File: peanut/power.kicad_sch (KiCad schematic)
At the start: 17 parts, among them J3 Battery JST, J4 Arming, Q5 PMOS, U4 MCP1826S, U5 TPS2116DRL

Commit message: feat: changed pressure sensor to BMP581
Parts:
- renumbered C15 to C16, C16 to C17, C17 to C18, C18 to C19, C19 to C20
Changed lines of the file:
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@@
 		(dnp no)
 		(fields_autoplaced yes)
-		(property "Reference" "C17"
+		(property "Reference" "C18"
 			(at 114.3 83.8199 0)
 			(show_name no)
@@
 			(project "peanut"
 				(path "/5c6b6cfc-6c84-425a-9b66-e6111713aae8/f944ce75-1da7-4030-9ed2-502ac98b17ed"
-					(reference "C17")
+					(reference "C18")
 					(unit 1)
 				)
@@
 		(dnp no)
 		(fields_autoplaced yes)
-		(property "Reference" "#PWR058"
+		(property "Reference" "#PWR061"
 			(at 232.41 80.01 0)
 			(hide yes)
@@
 			(project "peanut"
 				(path "/5c6b6cfc-6c84-425a-9b66-e6111713aae8/f944ce75-1da7-4030-9ed2-502ac98b17ed"
-					(reference "#PWR058")
+					(reference "#PWR061")
 					(unit 1)
 				)
@@
 		(dnp no)
 		(fields_autoplaced yes)
-		(property "Reference" "#PWR054"
+		(property "Reference" "#PWR057"
 			(at 163.83 77.47 0)
 			(hide yes)
@@
 			(project "peanut"
 				(path "/5c6b6cfc-6c84-425a-9b66-e6111713aae8/f944ce75-1da7-4030-9ed2-502ac98b17ed"
-					(reference "#PWR054")
+					(reference "#PWR057")
 					(unit 1)
 				)
@@
 		(dnp no)
 		(fields_autoplaced yes)
-		(property "Reference" "#PWR047"
+		(property "Reference" "#PWR050"
 			(at 105.41 72.39 0)
 			(hide yes)
@@
 			(project "peanut"
 				(path "/5c6b6cfc-6c84-425a-9b66-e6111713aae8/f944ce75-1da7-4030-9ed2-502ac98b17ed"
-					(reference "#PWR047")
+					(reference "#PWR050")
 					(unit 1)
 				)
@@
 		(dnp no)
 		(fields_autoplaced yes)
-		(property "Reference" "#PWR053"
+		(property "Reference" "#PWR056"
 			(at 139.7 92.71 0)
 			(hide yes)
@@
 			(project "peanut"
 				(path "/5c6b6cfc-6c84-425a-9b66-e6111713aae8/f944ce75-1da7-4030-9ed2-502ac98b17ed"
-					(reference "#PWR053")
+					(reference "#PWR056")
 					(unit 1)
 				)
@@
 		(in_pos_files yes)
 		(dnp no)
-		(property "Reference" "#PWR057"
+		(property "Reference" "#PWR060"
 			(at 231.14 71.12 0)
 			(hide yes)
@@
 			(project "peanut"
 				(path "/5c6b6cfc-6c84-425a-9b66-e6111713aae8/f944ce75-1da7-4030-9ed2-502ac98b17ed"
-					(reference "#PWR057")
+					(reference "#PWR060")
 					(unit 1)
 				)
@@
 		(dnp no)
 		(fields_autoplaced yes)
-		(property "Reference" "#PWR051"
+		(property "Reference" "#PWR054"
 			(at 116.84 140.97 0)
 			(hide yes)
@@
 			(project "peanut"
 				(path "/5c6b6cfc-6c84-425a-9b66-e6111713aae8/f944ce75-1da7-4030-9ed2-502ac98b17ed"
-					(reference "#PWR051")
+					(reference "#PWR054")
 					(unit 1)
 				)
@@
 		(in_pos_files yes)
 		(dnp no)
-		(property "Reference" "#PWR048"
+		(property "Reference" "#PWR051"
 			(at 105.41 83.82 0)
 			(hide yes)
@@
 			(project "peanut"
 				(path "/5c6b6cfc-6c84-425a-9b66-e6111713aae8/f944ce75-1da7-4030-9ed2-502ac98b17ed"
-					(reference "#PWR048")
+					(reference "#PWR051")
 					(unit 1)
 				)
@@
 		(dnp no)
 		(fields_autoplaced yes)
-		(property "Reference" "#PWR056"
+		(property "Reference" "#PWR059"
 			(at 199.39 71.12 0)
 			(hide yes)
@@
 			(project "peanut"
 				(path "/5c6b6cfc-6c84-425a-9b66-e6111713aae8/f944ce75-1da7-4030-9ed2-502ac98b17ed"
-					(reference "#PWR056")
+					(reference "#PWR059")
 					(unit 1)
 				)
@@
 		(in_pos_files yes)
 		(dnp no)
-		(property "Reference" "C15"
+		(property "Reference" "C16"
 			(at 45.212 71.12 0)
 			(show_name no)
@@
 			(project "peanut"
 				(path "/5c6b6cfc-6c84-425a-9b66-e6111713aae8/f944ce75-1da7-4030-9ed2-502ac98b17ed"
-					(reference "C15")
+					(reference "C16")
 					(unit 1)
 				)
@@
 		(in_pos_files yes)
 		(dnp no)
-		(property "Reference" "#PWR041"
+		(property "Reference" "#PWR044"
 			(at 43.18 102.87 0)
 			(hide yes)
@@
 			(project "peanut"
 				(path "/5c6b6cfc-6c84-425a-9b66-e6111713aae8/f944ce75-1da7-4030-9ed2-502ac98b17ed"
-					(reference "#PWR041")
+					(reference "#PWR044")
 					(unit 1)
 				)
@@
 		(dnp no)
 		(fields_autoplaced yes)
-		(property "Reference" "C18"
+		(property "Reference" "C19"
 			(at 121.92 73.6599 0)
 			(show_name no)
@@
 			(project "peanut"
 				(path "/5c6b6cfc-6c84-425a-9b66-e6111713aae8/f944ce75-1da7-4030-9ed2-502ac98b17ed"
-					(reference "C18")
+					(reference "C19")
 					(unit 1)
 				)
@@
 		(dnp no)
 		(fields_autoplaced yes)
-		(property "Reference" "#PWR055"
+		(property "Reference" "#PWR058"
 			(at 198.12 76.2 0)
 			(hide yes)
@@
 			(project "peanut"
 				(path "/5c6b6cfc-6c84-425a-9b66-e6111713aae8/f944ce75-1da7-4030-9ed2-502ac98b17ed"
-					(reference "#PWR055")
+					(reference "#PWR058")
 					(unit 1)
 				)
@@
 		(dnp no)
 		(fields_autoplaced yes)
-		(property "Reference" "#PWR052"
+		(property "Reference" "#PWR055"
 			(at 127 119.38 0)
 			(hide yes)
@@
 			(project "peanut"
 				(path "/5c6b6cfc-6c84-425a-9b66-e6111713aae8/f944ce75-1da7-4030-9ed2-502ac98b17ed"
-					(reference "#PWR052")
+					(reference "#PWR055")
 					(unit 1)
 				)
@@
 		(dnp no)
 		(fields_autoplaced yes)
-		(property "Reference" "#PWR046"
+		(property "Reference" "#PWR049"
 			(at 86.36 72.39 0)
 			(hide yes)
@@
 			(project "peanut"
 				(path "/5c6b6cfc-6c84-425a-9b66-e6111713aae8/f944ce75-1da7-4030-9ed2-502ac98b17ed"
-					(reference "#PWR046")
+					(reference "#PWR049")
 					(unit 1)
 				)
@@
 		(in_pos_files yes)
 		(dnp no)
-		(property "Reference" "#PWR049"
+		(property "Reference" "#PWR052"
 			(at 109.22 119.38 0)
 			(hide yes)
@@
 			(project "peanut"
 				(path "/5c6b6cfc-6c84-425a-9b66-e6111713aae8/f944ce75-1da7-4030-9ed2-502ac98b17ed"
-					(reference "#PWR049")
+					(reference "#PWR052")
 					(unit 1)
 				)
@@
 		(dnp no)
 		(fields_autoplaced yes)
-		(property "Reference" "#PWR045"
+		(property "Reference" "#PWR048"
 			(at 82.55 119.38 0)
 			(hide yes)
@@
 			(project "peanut"
 				(path "/5c6b6cfc-6c84-425a-9b66-e6111713aae8/f944ce75-1da7-4030-9ed2-502ac98b17ed"
-					(reference "#PWR045")
+					(reference "#PWR048")
 					(unit 1)
 				)
@@
 		(dnp no)
 		(fields_autoplaced yes)
-		(property "Reference" "C16"
+		(property "Reference" "C17"
 			(at 90.17 71.1199 0)
 			(show_name no)
@@
 			(project "peanut"
 				(path "/5c6b6cfc-6c84-425a-9b66-e6111713aae8/f944ce75-1da7-4030-9ed2-502ac98b17ed"
-					(reference "C16")
+					(reference "C17")
 					(unit 1)
 				)
@@
 		(dnp no)
 		(fields_autoplaced yes)
-		(property "Reference" "#PWR042"
+		(property "Reference" "#PWR045"
 			(at 53.34 114.3 0)
 			(hide yes)
@@
 			(project "peanut"
 				(path "/5c6b6cfc-6c84-425a-9b66-e6111713aae8/f944ce75-1da7-4030-9ed2-502ac98b17ed"
-					(reference "#PWR042")
+					(reference "#PWR045")
 					(unit 1)
 				)
@@
 		(dnp no)
 		(fields_autoplaced yes)
-		(property "Reference" "#PWR044"
+		(property "Reference" "#PWR047"
 			(at 82.55 101.6 0)
 			(hide yes)
@@
 			(project "peanut"
 				(path "/5c6b6cfc-6c84-425a-9b66-e6111713aae8/f944ce75-1da7-4030-9ed2-502ac98b17ed"
-					(reference "#PWR044")
+					(reference "#PWR047")
 					(unit 1)
 				)
@@
 		(dnp no)
 		(fields_autoplaced yes)
-		(property "Reference" "#PWR043"
+		(property "Reference" "#PWR046"
 			(at 67.31 83.82 0)
 			(hide yes)
@@
 			(project "peanut"
 				(path "/5c6b6cfc-6c84-425a-9b66-e6111713aae8/f944ce75-1da7-4030-9ed2-502ac98b17ed"
-					(reference "#PWR043")
+					(reference "#PWR046")
 					(unit 1)
 				)
@@
 		(dnp no)
 		(fields_autoplaced yes)
-		(property "Reference" "#PWR050"
+		(property "Reference" "#PWR053"
 			(at 114.3 95.25 0)
 			(hide yes)
@@
 			(project "peanut"
 				(path "/5c6b6cfc-6c84-425a-9b66-e6111713aae8/f944ce75-1da7-4030-9ed2-502ac98b17ed"
-					(reference "#PWR050")
+					(reference "#PWR053")
 					(unit 1)
 				)
@@
 		(dnp no)
 		(fields_autoplaced yes)
-		(property "Reference" "C19"
+		(property "Reference" "C20"
 			(at 157.48 74.9299 0)
 			(show_name no)
@@
 			(project "peanut"
 				(path "/5c6b6cfc-6c84-425a-9b66-e6111713aae8/f944ce75-1da7-4030-9ed2-502ac98b17ed"
-					(reference "C19")
+					(reference "C20")
 					(unit 1)
 				)

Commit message: feat: new routing done
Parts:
- R23: footprint Resistor_SMD:R_0402_1005Metric -> Resistor_SMD:R_0603_1608Metric; MPN ERA-2AED104X -> ERA-3AED104V
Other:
- note added: "LDO regulator"
- note removed: "Switching regulator"
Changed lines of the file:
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@@
 		)
 	)
-	(text "Switching regulator"
+	(text "LDO regulator"
 		(exclude_from_sim no)
 		(at 66.802 57.404 0)
@@
 	)
 	(junction
-		(at 83.82 68.58)
+		(at 110.49 81.28)
 		(diameter 0)
 		(color 0 0 0 0)
 	)
 	(junction
-		(at 110.49 81.28)
+		(at 227.33 69.85)
 		(diameter 0)
 		(color 0 0 0 0)
 	)
 	(junction
-		(at 227.33 69.85)
+		(at 53.34 99.06)
 		(diameter 0)
 		(color 0 0 0 0)
 	)
 	(junction
-		(at 53.34 99.06)
+		(at 195.58 69.85)
 		(diameter 0)
 		(color 0 0 0 0)
@@
 	(wire
 		(pts
-			(xy 83.82 68.58) (xy 86.36 68.58)
-		)
-		(stroke
-			(width 0)
-			(type default)
-		)
-	)
-	(wire
-		(pts
 			(xy 123.19 118.11) (xy 123.19 115.57)
 		)
@@
 	(wire
 		(pts
-			(xy 74.93 68.58) (xy 83.82 68.58)
+			(xy 74.93 68.58) (xy 86.36 68.58)
 		)
 		(stroke
@@
 	)
 	(symbol
-		(lib_id "power:VBUS")
-		(at 105.41 80.01 0)
+		(lib_id "power:PWR_FLAG")
+		(at 195.58 69.85 0)
 		(unit 1)
 		(body_style 1)
@@
 		(in_pos_files yes)
 		(dnp no)
-		(property "Reference" "#PWR051"
-			(at 105.41 83.82 0)
+		(fields_autoplaced yes)
+		(property "Reference" "#FLG02"
+			(at 195.58 67.945 0)
 			(hide yes)
 			(show_name no)
@@
 			)
 		)
-		(property "Value" "VBAT"
-			(at 105.41 74.93 0)
+		(property "Value" ""
+			(at 195.58 64.77 0)
 			(show_name no)
 			(do_not_autoplace no)
@@
 		)
 		(property "Footprint" ""
-			(at 105.41 80.01 0)
+			(at 195.58 69.85 0)
 			(hide yes)
 			(show_name no)
@@
 		)
 		(property "Datasheet" ""
-			(at 105.41 80.01 0)
+			(at 195.58 69.85 0)
 			(hide yes)
 			(show_name no)
@@
 			)
 		)
-		(property "Description" "Power symbol creates a global label with name \"VBUS\""
-			(at 105.41 80.01 0)
+		(property "Description" "Special symbol for telling ERC where power comes from"
+			(at 195.58 69.85 0)
 			(hide yes)
 			(show_name no)
@@
 			(project "peanut"
 				(path "/5c6b6cfc-6c84-425a-9b66-e6111713aae8/f944ce75-1da7-4030-9ed2-502ac98b17ed"
-					(reference "#PWR051")
+					(reference "#FLG02")
 					(unit 1)
 				)
@@
 	)
 	(symbol
-		(lib_id "power:PWR_FLAG")
-		(at 83.82 68.58 0)
+		(lib_id "power:VBUS")
+		(at 105.41 80.01 0)
 		(unit 1)
 		(body_style 1)
@@
 		(in_pos_files yes)
 		(dnp no)
-		(fields_autoplaced yes)
-		(property "Reference" "#FLG02"
-			(at 83.82 66.675 0)
+		(property "Reference" "#PWR051"
+			(at 105.41 83.82 0)
 			(hide yes)
 			(show_name no)
@@
 			)
 		)
-		(property "Value" "PWR_FLAG"
-			(at 83.82 63.5 0)
-			(hide yes)
+		(property "Value" "VBAT"
+			(at 105.41 74.93 0)
 			(show_name no)
 			(do_not_autoplace no)
@@
 		)
 		(property "Footprint" ""
-			(at 83.82 68.58 0)
+			(at 105.41 80.01 0)
 			(hide yes)
 			(show_name no)
@@
 		)
 		(property "Datasheet" ""
-			(at 83.82 68.58 0)
+			(at 105.41 80.01 0)
 			(hide yes)
 			(show_name no)
@@
 			)
 		)
-		(property "Description" "Special symbol for telling ERC where power comes from"
-			(at 83.82 68.58 0)
+		(property "Description" "Power symbol creates a global label with name \"VBUS\""
+			(at 105.41 80.01 0)
 			(hide yes)
 			(show_name no)
@@
 			(project "peanut"
 				(path "/5c6b6cfc-6c84-425a-9b66-e6111713aae8/f944ce75-1da7-4030-9ed2-502ac98b17ed"
-					(reference "#FLG02")
+					(reference "#PWR051")
 					(unit 1)
 				)
@@
 			)
 		)
-		(property "Footprint" "Resistor_SMD:R_0402_1005Metric"
+		(property "Footprint" "Resistor_SMD:R_0603_1608Metric"
 			(at 115.062 130.81 90)
 			(hide yes)
@@
 			)
 		)
-		(property "MPN" "ERA-2AED104X"
+		(property "MPN" "ERA-3AED104V"
 			(at 116.84 130.81 0)
 			(hide yes)

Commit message: chore: resolve DRC errors
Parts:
- D6: footprint Diode_SMD:D_SOD-323 -> Diode_SMD:D_SOD-323_HandSoldering
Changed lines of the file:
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@@
 			)
 		)
-		(property "Footprint" "Diode_SMD:D_SOD-323"
+		(property "Footprint" "Diode_SMD:D_SOD-323_HandSoldering"
 			(at 123.19 121.92 0)
 			(hide yes)

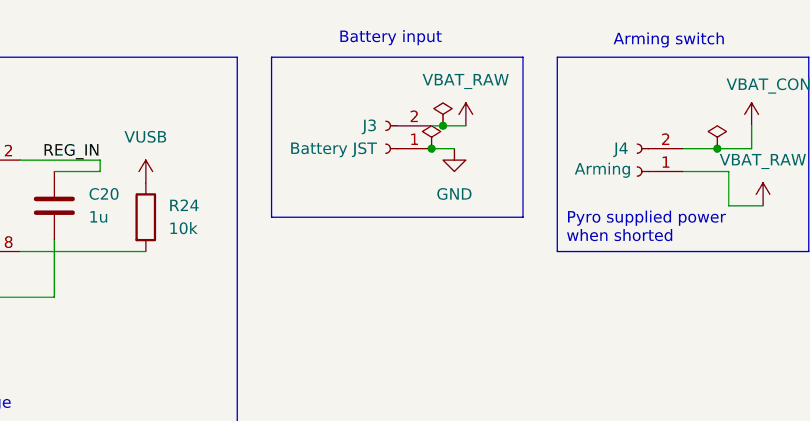
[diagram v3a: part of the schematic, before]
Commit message: feat: finished review; swapped battery lead polarity to match other rocket electronics
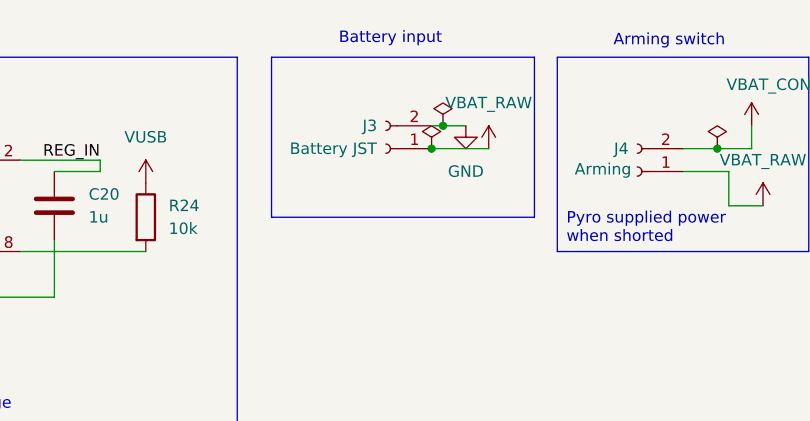
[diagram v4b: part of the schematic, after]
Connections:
- net GND: now also J3.2 (Pin_2); no longer J3.1 (Pin_1)
- net VBAT_RAW: now also J3.1 (Pin_1); no longer J3.2 (Pin_2)
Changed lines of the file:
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@@
 	(rectangle
 		(start 177.8 59.69)
-		(end 205.74 77.47)
+		(end 207.01 77.47)
 		(stroke
 			(width 0)
@@
 	)
 	(junction
+		(at 195.58 69.85)
+		(diameter 0)
+		(color 0 0 0 0)
+	)
+	(junction
 		(at 123.19 115.57)
 		(diameter 0)
@@
 	)
 	(junction
-		(at 195.58 69.85)
-		(diameter 0)
-		(color 0 0 0 0)
-	)
-	(junction
 		(at 67.31 76.2)
 		(diameter 0)
@@
 	(wire
 		(pts
-			(xy 198.12 69.85) (xy 195.58 69.85)
+			(xy 195.58 69.85) (xy 201.93 69.85)
 		)
 		(stroke
@@
 	(symbol
 		(lib_id "power:VBUS")
-		(at 199.39 67.31 0)
+		(at 201.93 69.85 0)
 		(unit 1)
 		(body_style 1)
@@
 		(fields_autoplaced yes)
 		(property "Reference" "#PWR059"
-			(at 199.39 71.12 0)
+			(at 201.93 73.66 0)
 			(hide yes)
 			(show_name no)
@@
 		)
 		(property "Value" "VBAT_RAW"
-			(at 199.39 62.23 0)
+			(at 201.93 64.77 0)
 			(show_name no)
 			(do_not_autoplace no)
@@
 		)
 		(property "Footprint" ""
-			(at 199.39 67.31 0)
+			(at 201.93 69.85 0)
 			(hide yes)
 			(show_name no)
@@
 		)
 		(property "Datasheet" ""
-			(at 199.39 67.31 0)
+			(at 201.93 69.85 0)
 			(hide yes)
 			(show_name no)
@@
 		)
 		(property "Description" "Power symbol creates a global label with name \"VBUS\""
-			(at 199.39 67.31 0)
+			(at 201.93 69.85 0)
 			(hide yes)
 			(show_name no)
@@
 				(path "/5c6b6cfc-6c84-425a-9b66-e6111713aae8/f944ce75-1da7-4030-9ed2-502ac98b17ed"
 					(reference "#PWR059")
+					(unit 1)
+				)
+			)
+		)
+	)
+	(symbol
+		(lib_id "power:GND")
+		(at 199.39 67.31 0)
+		(unit 1)
+		(body_style 1)
+		(exclude_from_sim no)
+		(in_bom yes)
+		(on_board yes)
+		(in_pos_files yes)
+		(dnp no)
+		(fields_autoplaced yes)
+		(property "Reference" "#PWR058"
+			(at 199.39 73.66 0)
+			(hide yes)
+			(show_name no)
+			(do_not_autoplace no)
+			(effects
+				(font
+					(size 1.27 1.27)
+				)
+			)
+		)
+		(property "Value" "GND"
+			(at 199.39 72.39 0)
+			(show_name no)
+			(do_not_autoplace no)
+			(effects
+				(font
+					(size 1.27 1.27)
+				)
+			)
+		)
+		(property "Footprint" ""
+			(at 199.39 67.31 0)
+			(hide yes)
+			(show_name no)
+			(do_not_autoplace no)
+			(effects
+				(font
+					(size 1.27 1.27)
+				)
+			)
+		)
+		(property "Datasheet" ""
+			(at 199.39 67.31 0)
+			(hide yes)
+			(show_name no)
+			(do_not_autoplace no)
+			(effects
+				(font
+					(size 1.27 1.27)
+				)
+			)
+		)
+		(property "Description" "Power symbol creates a global label with name \"GND\" , ground"
+			(at 199.39 67.31 0)
+			(hide yes)
+			(show_name no)
+			(do_not_autoplace no)
+			(effects
+				(font
+					(size 1.27 1.27)
+				)
+			)
+		)
+		(pin "1"
+		)
+		(instances
+			(project "peanut"
+				(path "/5c6b6cfc-6c84-425a-9b66-e6111713aae8/f944ce75-1da7-4030-9ed2-502ac98b17ed"
+					(reference "#PWR058")
 					(unit 1)
 				)
@@
 					(unit 1)
 				)
-			)
-		)
-	)
-	(symbol
-		(lib_id "power:GND")
-		(at 198.12 69.85 0)
-		(unit 1)
-		(body_style 1)
-		(exclude_from_sim no)
-		(in_bom yes)
-		(on_board yes)
-		(in_pos_files yes)
-		(dnp no)
-		(fields_autoplaced yes)
-		(property "Reference" "#PWR058"
-			(at 198.12 76.2 0)
-			(hide yes)
-			(show_name no)
-			(do_not_autoplace no)
-			(effects
-				(font
-					(size 1.27 1.27)
-				)
-			)
-		)
-		(property "Value" "GND"
-			(at 198.12 74.93 0)
-			(show_name no)
-			(do_not_autoplace no)
-			(effects
-				(font
-					(size 1.27 1.27)
-				)
-			)
-		)
-		(property "Footprint" ""
-			(at 198.12 69.85 0)
-			(hide yes)
-			(show_name no)
-			(do_not_autoplace no)
-			(effects
-				(font
-					(size 1.27 1.27)
-				)
-			)
-		)
-		(property "Datasheet" ""
-			(at 198.12 69.85 0)
-			(hide yes)
-			(show_name no)
-			(do_not_autoplace no)
-			(effects
-				(font
-					(size 1.27 1.27)
-				)
-			)
-		)
-		(property "Description" "Power symbol creates a global label with name \"GND\" , ground"
-			(at 198.12 69.85 0)
-			(hide yes)
-			(show_name no)
-			(do_not_autoplace no)
-			(effects
-				(font
-					(size 1.27 1.27)
-				)
-			)
-		)
-		(pin "1"
-		)
-		(instances
-			(project "peanut"
-				(path "/5c6b6cfc-6c84-425a-9b66-e6111713aae8/f944ce75-1da7-4030-9ed2-502ac98b17ed"
-					(reference "#PWR058")
-					(unit 1)
-				)
